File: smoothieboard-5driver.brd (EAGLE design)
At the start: 129.5 x 105.1 mm, 281 parts, among them IC1 LPC1769, IC10 LM1117-3.3V, IC11 78L12F, IC12 A4982, IC13 R-78E-5.0, IC2 A4982, IC3 A4982, IC4 MCP44X1, IC5 A4982, IC6 A4982, IC9 MCP44X1, J10 POWER_JACKSMD, Q1 BSL207SP, Q10 SUD50P04-08-GE3, Q2 12MHz, Q3 25MHz, Q4 ZXMN4A06, Q5 AOT240L, Q6 AOT240L, Q7 AOT240L, Q8 ZXMN4A06, Q9 ZXMN4A06, U1 USD-SOCKETNEW, X14 USBPTH

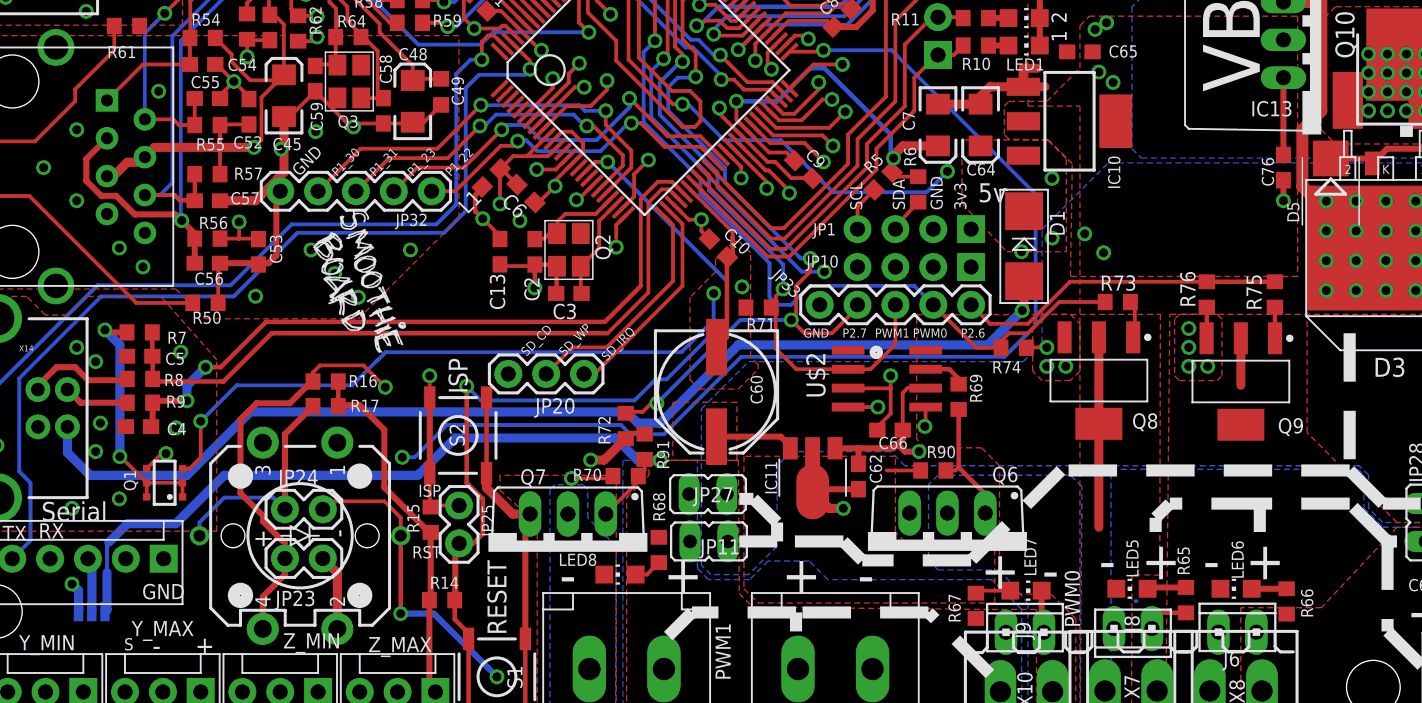
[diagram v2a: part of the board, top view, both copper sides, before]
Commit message: UART voltage selector- add trace to select 5v by default, user must cut trace to select 3.3v
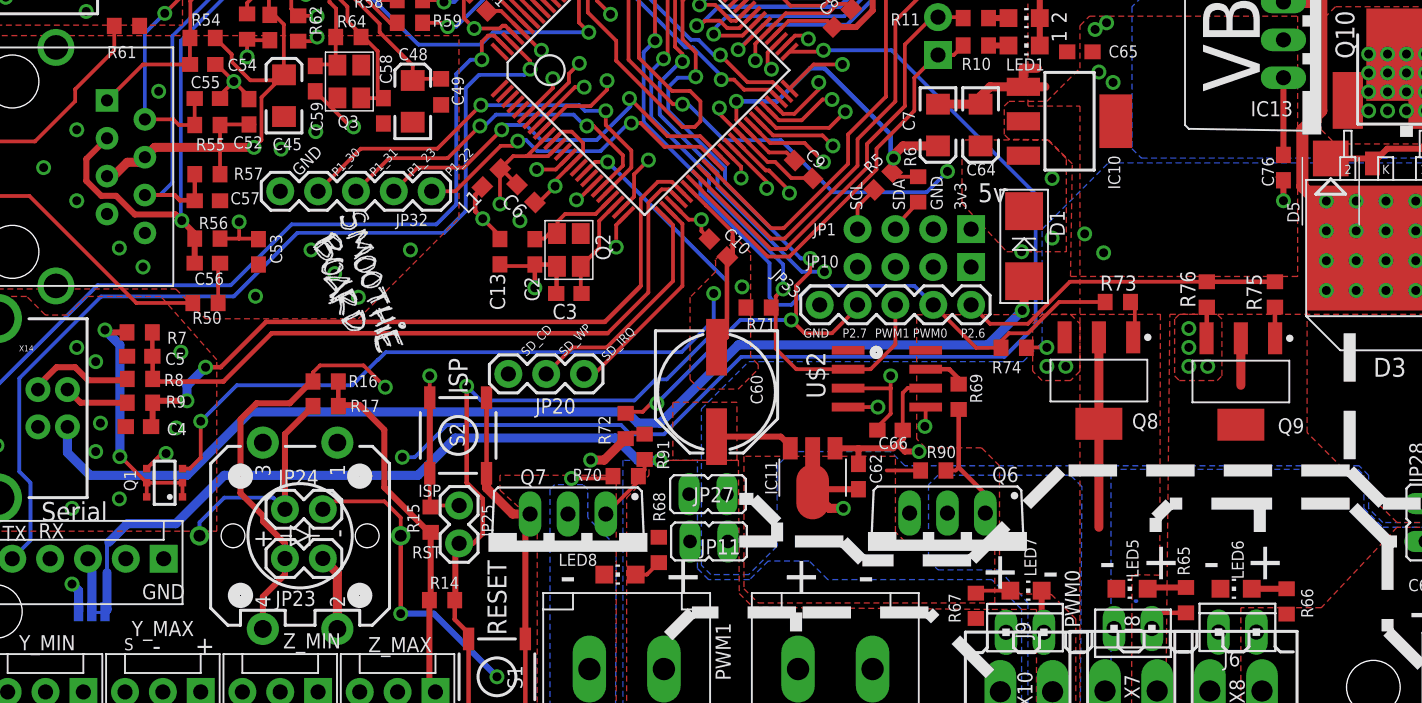
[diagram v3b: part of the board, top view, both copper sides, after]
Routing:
- net GND: track 292.4 -> 265.1 mm
- net N$114: track 0.00 -> 0.95 mm
- net VBB: track 306.4 -> 307.0 mm
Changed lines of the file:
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@@
 <wire x1="30.4555" y1="46.267" x2="29.464" y2="46.267" width="0.254" layer="1"/>
 <wire x1="28.5115" y1="41.2085" x2="28.914" y2="41.2085" width="0.254" layer="1"/>
-<wire x1="28.914" y1="41.2085" x2="30.607" y2="42.9015" width="0.254" layer="1"/>
 <wire x1="26.035" y1="45.212" x2="26.035" y2="46.394" width="0.254" layer="1"/>
 <wire x1="27.559" y1="46.3305" x2="26.0985" y2="46.3305" width="0.254" layer="1"/>
@@
 <wire x1="33.97" y1="59.67" x2="33.97" y2="59.0249" width="0.254" layer="1"/>
 <wire x1="30.607" y1="42.9015" x2="32.766" y2="40.7425" width="0.254" layer="1"/>
-<wire x1="32.766" y1="40.7425" x2="35.179" y2="40.7425" width="0.254" layer="1"/>
-<wire x1="39.0525" y1="41.9875" x2="37.8925" y2="40.8275" width="0.254" layer="1"/>
-<wire x1="37.8925" y1="40.8275" x2="37.1475" y2="40.8275" width="0.254" layer="1"/>
-<wire x1="37.1475" y1="40.8275" x2="37.0625" y2="40.7425" width="0.254" layer="1"/>
-<wire x1="37.0625" y1="40.7425" x2="35.179" y2="40.7425" width="0.254" layer="1"/>
 <wire x1="24.091" y1="28.702" x2="24.091" y2="31.242" width="0.254" layer="1"/>
 <wire x1="24.091" y1="31.242" x2="24.218" y2="31.369" width="0.254" layer="1"/>
@@
 <wire x1="32.091" y1="6.831" x2="32.091" y2="10.581" width="0.6096" layer="1"/>
 <wire x1="32.091" y1="10.581" x2="31.115" y2="11.557" width="0.6096" layer="1"/>
-<wire x1="28.5115" y1="41.2085" x2="28.5115" y2="37.465" width="0.6096" layer="1"/>
-<wire x1="28.5115" y1="37.465" x2="28.067" y2="37.0205" width="0.6096" layer="1"/>
-<wire x1="26.709" y1="31.369" x2="26.797" y2="31.281" width="0.4064" layer="1"/>
-<wire x1="26.709" y1="31.369" x2="27.479" y2="31.369" width="0.4064" layer="1"/>
-<wire x1="27.479" y1="31.369" x2="28" y2="31.89" width="0.4064" layer="1"/>
-<wire x1="28" y1="31.89" x2="28" y2="36.9535" width="0.4064" layer="1"/>
-<wire x1="28" y1="36.9535" x2="28.067" y2="37.0205" width="0.4064" layer="1"/>
-<wire x1="26.709" y1="31.369" x2="24.218" y2="31.369" width="0.4064" layer="1"/>
 <wire x1="42.1005" y1="17.272" x2="42.1005" y2="16.2895" width="0.6096" layer="1"/>
 <wire x1="42.1005" y1="16.2895" x2="43.8485" y2="14.5415" width="0.6096" layer="1"/>
@@
 <contactref element="IC11" pad="2@1"/>
 <wire x1="63.98" y1="16.03" x2="63.98" y2="18.697" width="0.4064" layer="1"/>
-<wire x1="24.218" y1="35.56" x2="26.6065" y2="35.56" width="0.6096" layer="1"/>
-<wire x1="26.6065" y1="35.56" x2="28.067" y2="37.0205" width="0.6096" layer="1"/>
 <contactref element="X14" pad="GND"/>
 <polygon width="0.254" layer="1" spacing="0.254" isolate="0.254">
@@
 <wire x1="98.1075" y1="49.2125" x2="97.79" y2="48.895" width="0.8128" layer="1"/>
 <wire x1="97.79" y1="48.895" x2="95.5675" y2="48.895" width="0.8128" layer="1"/>
-<wire x1="98.445" y1="33.5375" x2="98.7425" y2="33.995" width="0" layer="19" extent="1-1"/>
+<wire x1="98.7425" y1="33.995" x2="98.7425" y2="33.835" width="0.2032" layer="1"/>
+<wire x1="98.7425" y1="33.835" x2="98.445" y2="33.5375" width="0.2032" layer="1"/>
 </signal>
 <signal name="P0W">
@@
 <wire x1="101.21" y1="38.395" x2="101.5425" y2="38.0625" width="0.4064" layer="1"/>
 </signal>
+<signal name="N$114">
+<wire x1="15.5575" y1="7.9375" x2="16.51" y2="7.9375" width="0.2032" layer="16"/>
+</signal>
 </signals>

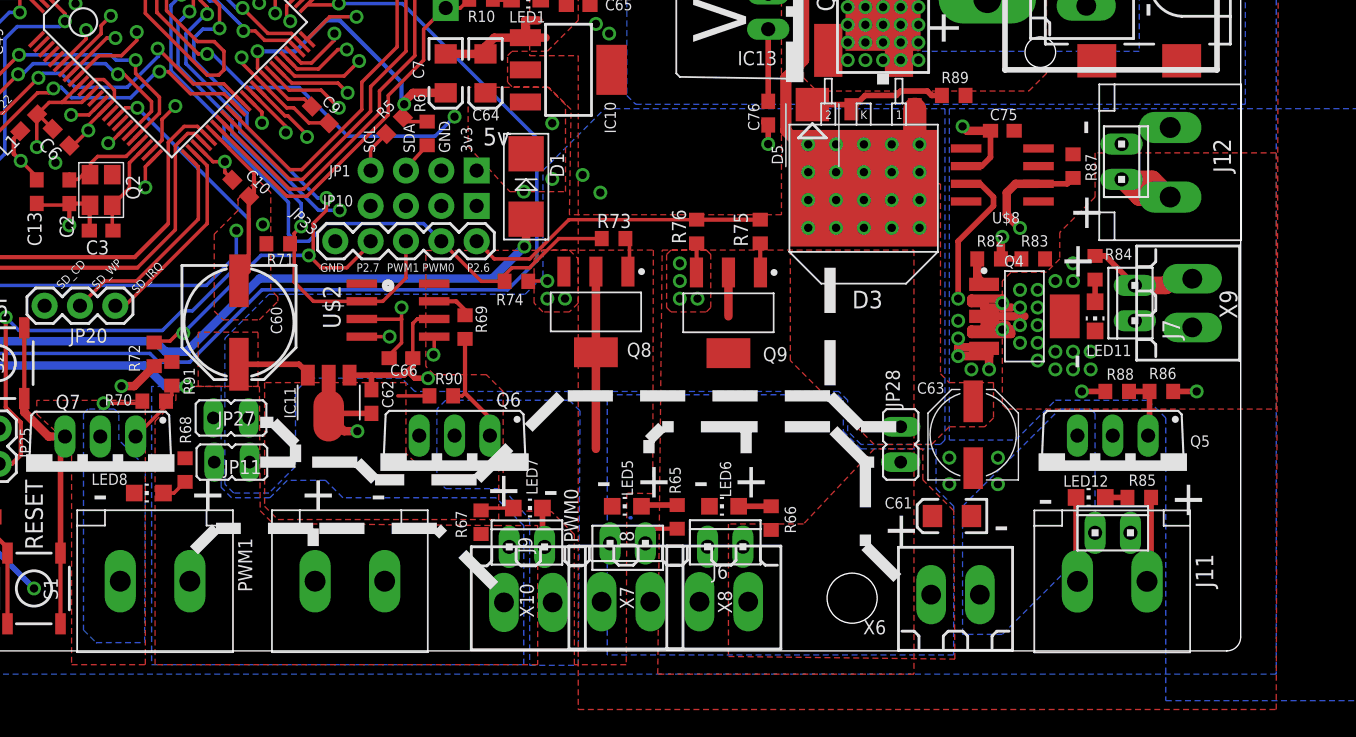
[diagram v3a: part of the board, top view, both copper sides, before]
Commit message: ensure all connectors include a 3.5mm footprint, remove 0.1" footprint from high current connector, minor routing updates
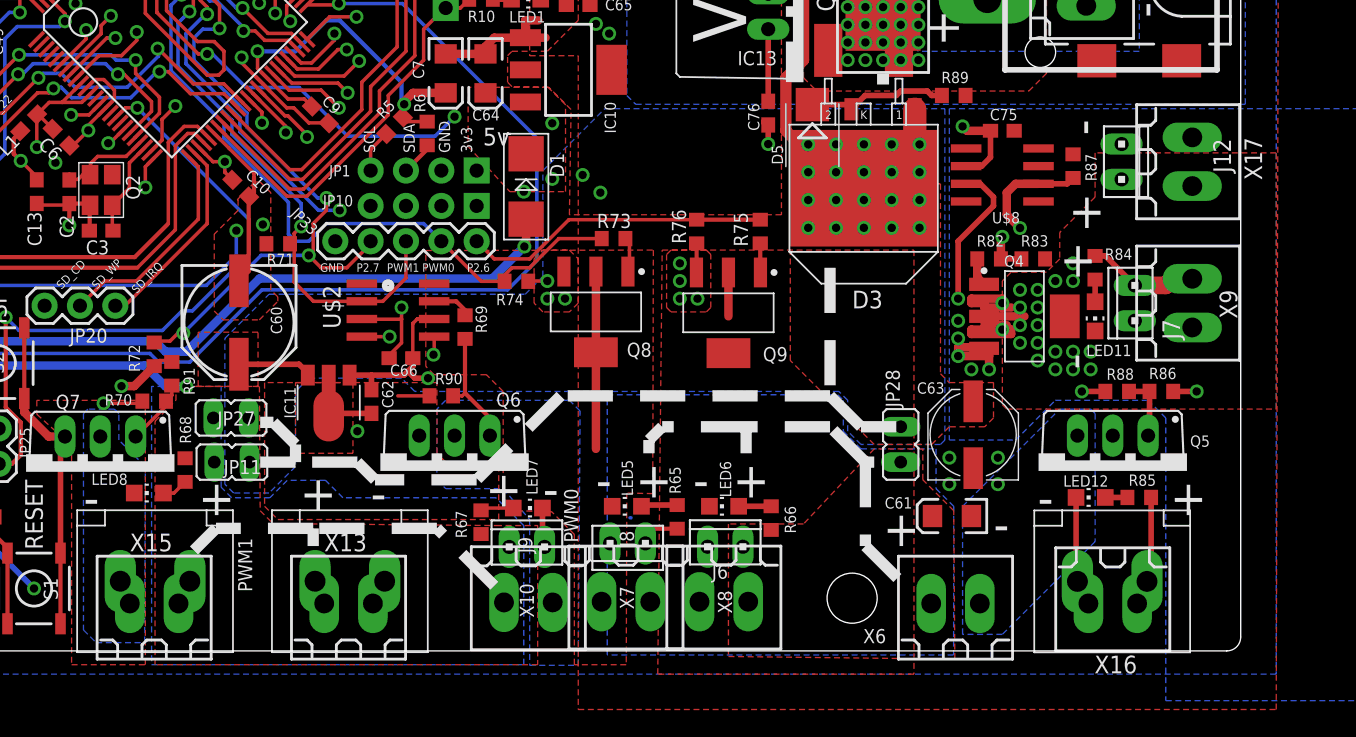
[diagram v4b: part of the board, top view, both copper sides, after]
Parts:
- removed J11: (no value), con-amp:10X02MTA
- removed U$9: 5MMCONN, eric_sorensen:1715250000
- added X13, X15, X16, X17: (no value), con-weidmueller-sl35:180G-2
- moved X6 0.63 mm to (109.0, 2.54)
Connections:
- net GND: now also X13.2, X17.1; no longer U$9.P$2
- net MOSFET_DRIVE: now also X13.1, X15.2
- net MOSFET_DRIVE1: now also X16.1, X17.2; no longer J11.1, U$9.P$1
- net N$109: now also X16.2; no longer J11.2
- net N$94: now also X15.1
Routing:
- net MOSFET_DRIVE1: track 22.3 -> 14.3 mm
- net GND: track 265.1 -> 262.6 mm

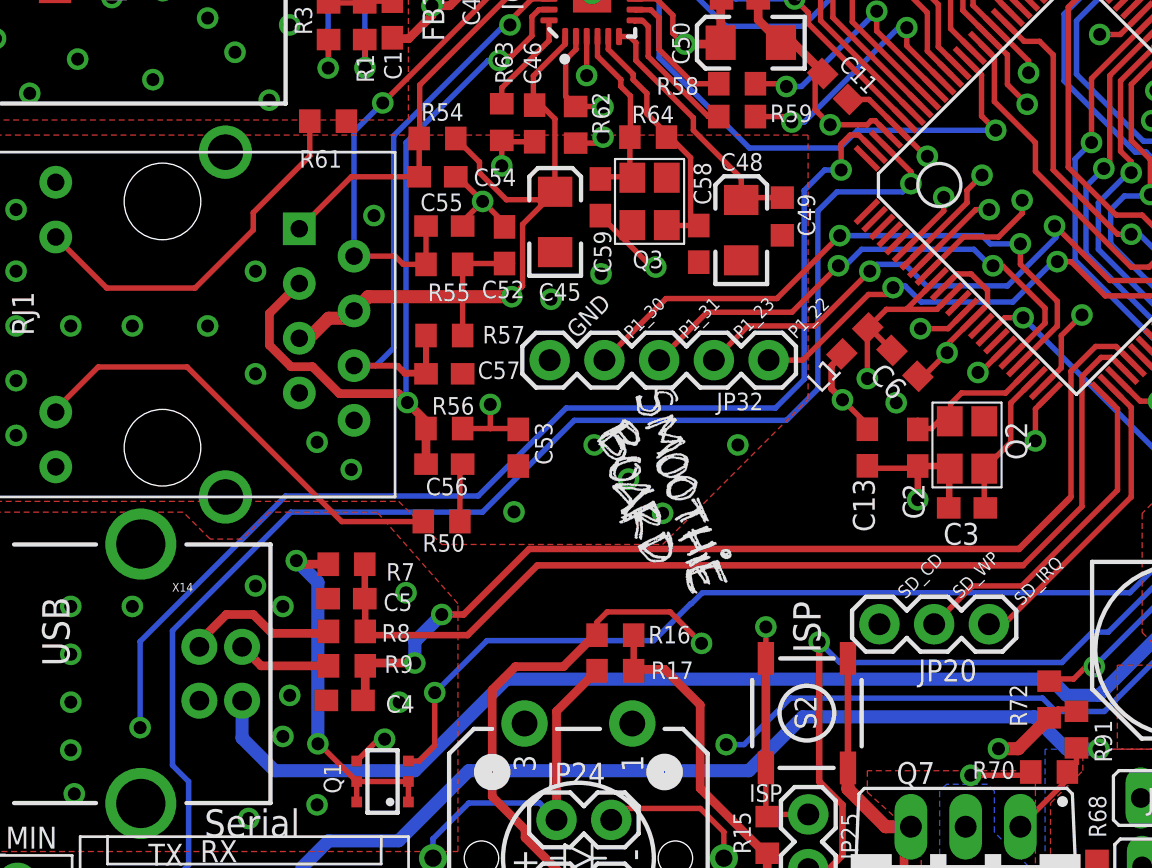
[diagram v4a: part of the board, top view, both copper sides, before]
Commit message: add solder pads for JTAG- not enough room to route a proper connector
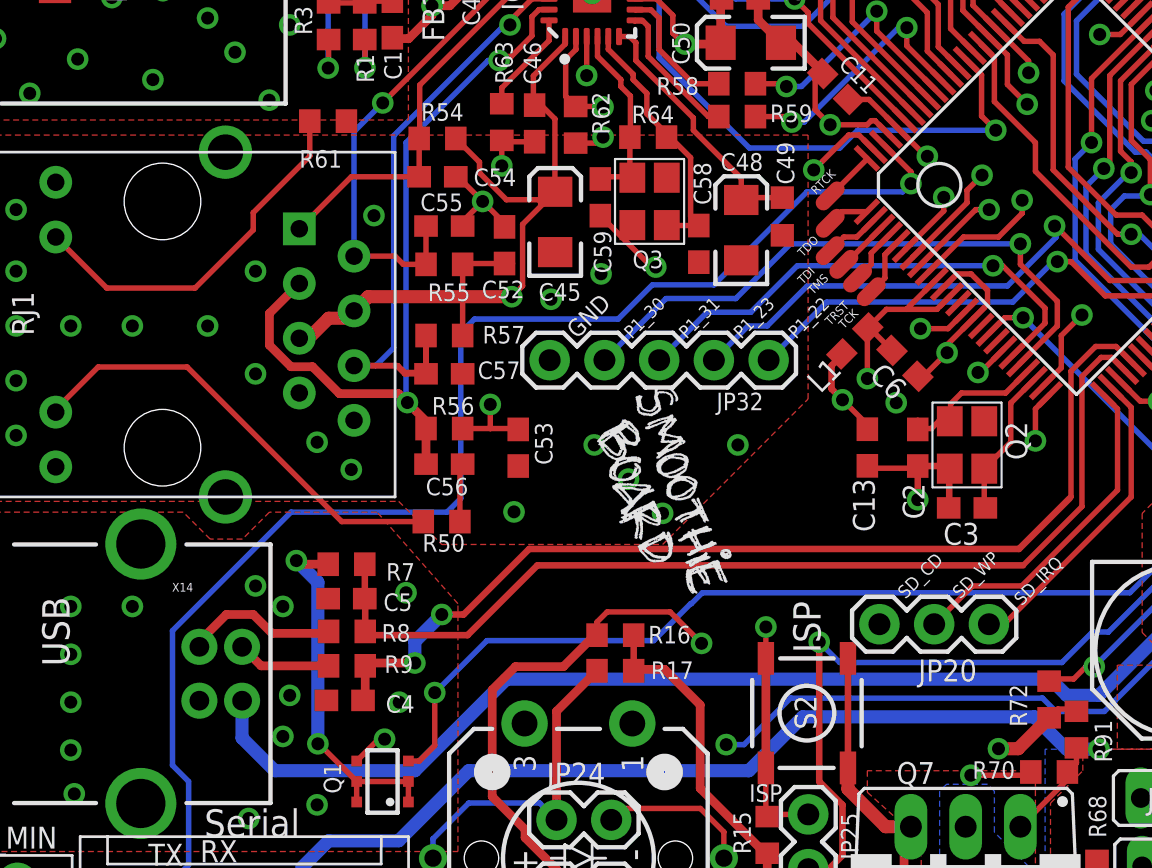
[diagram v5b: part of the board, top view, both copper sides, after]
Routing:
- net JTAG-TCK: track 0.00 -> 3.25 mm
- net JTAG-TDI: track 0.00 -> 3.11 mm
- net JTAG-TRST: track 0.00 -> 3.09 mm
- net JTAG-TMS: track 0.00 -> 2.95 mm
- net JTAG-RTCK: track 0.00 -> 2.90 mm
- net RX_0: track 63.8 -> 61.1 mm, vias 2 -> 1
- net JTAG-TDO: track 0.00 -> 2.38 mm
- net RSTOUT: track 37.1 -> 34.9 mm
- net AVCC: track 76.2 -> 75.1 mm
- net P1_23: track 117.3 -> 116.5 mm, vias 4 -> 3
- net P1_31: track 24.0 -> 23.4 mm, vias 2 -> 1
- net P1_22: track 106.9 -> 106.3 mm, vias 4 -> 3
- net P1_30: track 28.9 -> 28.6 mm, vias 2 -> 1
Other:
- board text added: "RTCK"
- board text added: "TCK"
- board text added: "TDI"
- board text added: "TDO"
- board text added: "TMS"
- board text added: "TRST"

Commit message: reduce I2C pull-up resistors to 2.2k
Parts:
- R35, R36, R5, R6: value 10K -> 2.2k
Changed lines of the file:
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@@
 <attribute name="VALUE" x="37.846" y="19.1135" size="1.27" layer="27" rot="R270"/>
 </element>
-<element name="R5" library="resistor" package="R0603" value="10K" x="68.71435" y="36.8886875" smashed="yes" rot="R45">
+<element name="R5" library="resistor" package="R0603" value="2.2k" x="68.71435" y="36.8886875" smashed="yes" rot="R45">
 <attribute name="NAME" x="67.8933625" y="37.3151375" size="0.8128" layer="25" rot="R45"/>
 <attribute name="VALUE" x="68.893953125" y="34.01500625" size="1.27" layer="27" rot="R45"/>
 </element>
-<element name="R6" library="resistor" package="R0603" value="10K" x="71.0565" y="36.322" smashed="yes" rot="R90">
+<element name="R6" library="resistor" package="R0603" value="2.2k" x="71.0565" y="36.322" smashed="yes" rot="R90">
 <attribute name="NAME" x="70.9295" y="37.846" size="0.8128" layer="25" rot="R90"/>
 <attribute name="VALUE" x="73.2155" y="34.671" size="1.27" layer="27" rot="R90"/>
@@
 <attribute name="VALUE" x="57.1858" y="65.1383" size="1.016" layer="27" ratio="10" rot="R270"/>
 </element>
-<element name="R35" library="resistor" package="R0603" value="10K" x="69.469" y="64.77" smashed="yes">
+<element name="R35" library="resistor" package="R0603" value="2.2k" x="69.469" y="64.77" smashed="yes">
 <attribute name="NAME" x="71.247" y="64.516" size="0.8128" layer="25"/>
 <attribute name="VALUE" x="70.993" y="64.389" size="1.27" layer="27"/>
 </element>
-<element name="R36" library="resistor" package="R0603" value="10K" x="69.469" y="63.1825" smashed="yes">
+<element name="R36" library="resistor" package="R0603" value="2.2k" x="69.469" y="63.1825" smashed="yes">
 <attribute name="NAME" x="71.3105" y="62.9285" size="0.8128" layer="25"/>
 <attribute name="VALUE" x="71.247" y="62.9285" size="1.27" layer="27"/>
@@
 </signal>
 </signals>
-<errors>
-</errors>
 </board>
 </drawing>

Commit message: Break out digipot I2C bus to a header
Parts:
- added JP8: (no value), SparkFun:1X04_NO_SILK
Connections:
- net 3.3V: now also JP8.1
- net GND: now also JP8.2
- net POT_SCL: now also JP8.4
- net POT_SDA: now also JP8.3
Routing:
- net POT_SDA: track 70.8 -> 71.7 mm
- net POT_SCL: track 69.2 -> 70.2 mm
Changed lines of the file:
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@@
 <text x="41.275" y="37.7825" size="0.4064" layer="121" font="vector" ratio="15" rot="R45">TRST</text>
 <text x="41.91" y="37.62375" size="0.4064" layer="121" font="vector" ratio="15" rot="R45">TCK</text>
+<text x="86.0425" y="47.9425" size="0.8128" layer="121" ratio="15" rot="R315">3v3</text>
+<text x="86.0425" y="50.4825" size="0.8128" layer="121" ratio="15" rot="R315">GND</text>
+<text x="86.0425" y="52.705" size="0.8128" layer="121" ratio="15" rot="R315">SDA</text>
+<text x="86.0425" y="55.5625" size="0.8128" layer="121" ratio="15" rot="R315">SCL</text>
 </plain>
 <attributes>
@@
 <attribute name="OC_FARNELL" value="unknown" x="126.0475" y="34.29" size="1.778" layer="27" rot="R270" display="off"/>
 </element>
+<element name="JP8" library="SparkFun" package="1X04_NO_SILK" value="" x="85.4075" y="48.895" rot="R90"/>
 </elements>
 <signals>
@@
 <vertex x="61.595" y="13.335"/>
 </polygon>
+<contactref element="JP8" pad="2"/>
 </signal>
 <signal name="3.3V">
@@
 <wire x1="71.0565" y1="37.172" x2="69.63311875" y2="37.172" width="0.254" layer="1"/>
 <wire x1="69.63311875" y1="37.172" x2="69.315390625" y2="37.489728125" width="0.254" layer="1"/>
+<contactref element="JP8" pad="1"/>
 </signal>
 <signal name="AVCC">
@@
 <wire x1="88.265" y1="55.5625" x2="89.2175" y2="55.5625" width="0.3048" layer="1"/>
 <wire x1="89.2175" y1="55.5625" x2="89.8525" y2="56.1975" width="0.3048" layer="1"/>
-<wire x1="88.265" y1="55.5625" x2="78.74" y2="55.5625" width="0.3048" layer="15"/>
+<wire x1="88.265" y1="55.5625" x2="85.4075" y2="55.5625" width="0.3048" layer="15"/>
+<wire x1="85.4075" y1="55.5625" x2="78.74" y2="55.5625" width="0.3048" layer="15"/>
 <wire x1="78.74" y1="55.5625" x2="71.4375" y2="62.865" width="0.3048" layer="15"/>
 <wire x1="71.4375" y1="62.865" x2="71.12" y2="62.865" width="0.3048" layer="15"/>
@@
 <wire x1="66.3575" y1="64.77" x2="66.3575" y2="63.373" width="0.3048" layer="15"/>
 <wire x1="66.3575" y1="63.373" x2="66.802" y2="62.9285" width="0.3048" layer="15"/>
+<contactref element="JP8" pad="4"/>
+<wire x1="85.4075" y1="56.515" x2="85.4075" y2="55.5625" width="0.3048" layer="15"/>
 </signal>
 <signal name="POT_SDA">
@@
 <wire x1="88.265" y1="54.2925" x2="87.9475" y2="54.2925" width="0.3048" layer="15"/>
 <wire x1="87.9475" y1="54.2925" x2="87.3125" y2="54.9275" width="0.3048" layer="15"/>
-<wire x1="87.3125" y1="54.9275" x2="78.4225" y2="54.9275" width="0.3048" layer="15"/>
+<wire x1="87.3125" y1="54.9275" x2="85.4075" y2="54.9275" width="0.3048" layer="15"/>
+<wire x1="85.4075" y1="54.9275" x2="78.4225" y2="54.9275" width="0.3048" layer="15"/>
 <wire x1="78.4225" y1="54.9275" x2="71.12" y2="62.23" width="0.3048" layer="15"/>
 <wire x1="71.12" y1="62.23" x2="70.8025" y2="62.23" width="0.3048" layer="15"/>
 <wire x1="70.8025" y1="62.23" x2="68.58" y2="64.4525" width="0.3048" layer="15"/>
 <wire x1="68.58" y1="64.4525" x2="67.2465" y2="64.4525" width="0.3048" layer="15"/>
+<contactref element="JP8" pad="3"/>
+<wire x1="85.4075" y1="53.975" x2="85.4075" y2="54.9275" width="0.3048" layer="15"/>
 </signal>
 <signal name="P1_22">
